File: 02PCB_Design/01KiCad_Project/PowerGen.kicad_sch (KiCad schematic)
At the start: 29 parts, among them J3 RS Pro 304-02-818, J4 RS Pro 304-02-818, U3 L6982C50DR, U4 AP2114D

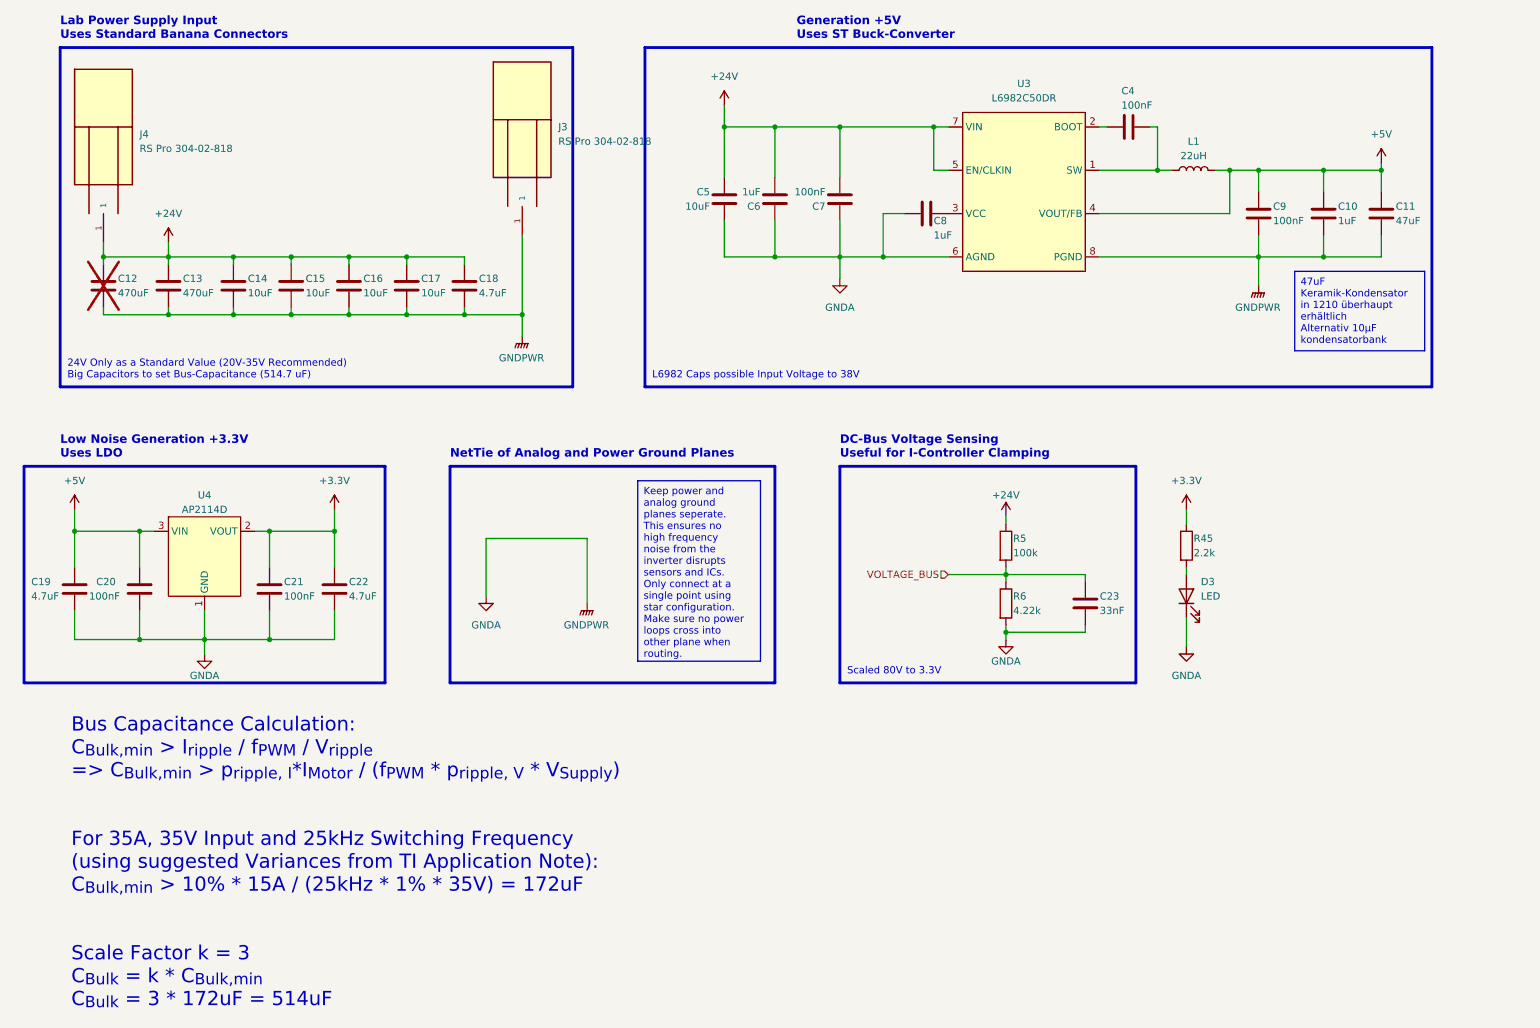
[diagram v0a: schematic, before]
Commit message: added ideal diode in schematic
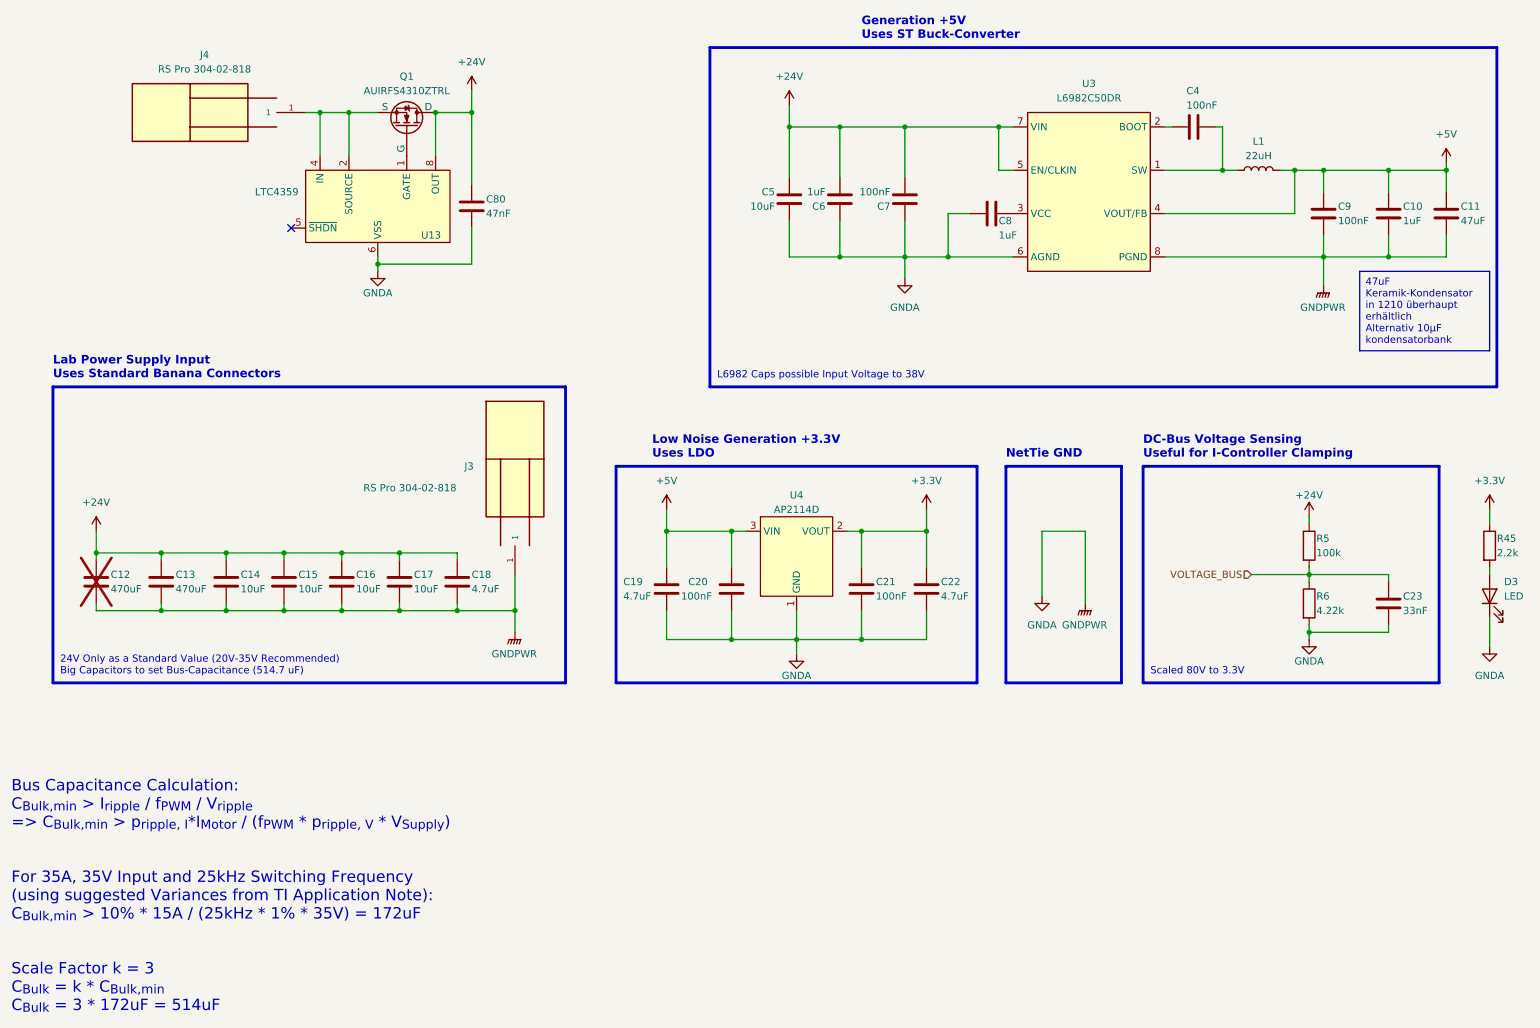
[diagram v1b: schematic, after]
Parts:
- added C80: 47nF, Capacitor_SMD:C_0603_1608Metric_Pad1.08x0.95mm_HandSolder, symbol Device:C
- added Q1: AUIRFS4310ZTRL, Package_TO_SOT_SMD:TO-263-2, symbol Simulation_SPICE:NMOS
- added U13: LTC4359, Package_SO:SO-8_3.9x4.9mm_P1.27mm, symbol MyKiCadLib:LTC4359
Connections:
- net +24V: now also C80.1, Q1.D, U13.8 (OUT); no longer J4.1
- net GNDA: now also C80.2, U13.6 (VSS)
- new net: Q1.G, U13.1 (GATE)
- new net: J4.1, Q1.S, U13.2 (SOURCE), U13.4 (IN)
- no-connect marks 0 -> 1
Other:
- note added: "NetTie GND"
- note removed: "NetTie of Analog and Power Ground Planes"
- moved on the sheet: C10, C11, C12, C13, C14, C15, C16, C17, C18, C19, C20, C21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

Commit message: Final V1
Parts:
- U3: footprint Package_SO:TSSOP-8_3x3mm_P0.65mm -> Package_SO:SO-8_3.9x4.9mm_P1.27mm
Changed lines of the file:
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@@
       (effects (font (size 1.27 1.27)))
     )
-    (property "Footprint" "Package_SO:TSSOP-8_3x3mm_P0.65mm" (at 209.55 35.56 0)
+    (property "Footprint" "Package_SO:SO-8_3.9x4.9mm_P1.27mm" (at 209.55 35.56 0)
       (effects (font (size 1.27 1.27)) hide)
     )

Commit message: Final v2 & Fertigung
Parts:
- Q1: value AUIRFS4310ZTRL -> IPB020N10N5
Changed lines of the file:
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@@
       (effects (font (size 1.27 1.27)))
     )
-    (property "Value" "AUIRFS4310ZTRL" (at 85.09 33.02 90)
+    (property "Value" "IPB020N10N5" (at 85.09 33.02 90)
       (effects (font (size 1.27 1.27)))
     )
